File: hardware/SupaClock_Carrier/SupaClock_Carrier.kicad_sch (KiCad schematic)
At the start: 27 parts, among them J11 AD8232_SparkFun, J12_LA1 ECG_LA_pad_M3, J12_RA1 ECG_RA_pad_M3, J12_RL1 ECG_RL_pad_M3, J13 AD8232_Pads_RA_LA_RL, J14 MAX30102_bot, J15 XIAO_BAT_Wires, J3 MAX30102_top, J4 MAX30205_8pad, J5 BMI160_7p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

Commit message: Add DRC JSON files for SupaClock Carrier: drc_post_relax.json and drc_post_thtswap.json
- Created drc_post_relax.json with 509 violations and warnings related to thermal relief, text dimensions, and footprint mismatches.
- Created drc_post_thtswap.json with 653 violations and warnings, including unconnected items, hole size issues, and silkscreen clearance violations.
- Both files include ignored checks and are formatted according to the KiCad DRC schema.
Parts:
- C2: footprint Capacitor_SMD:C_0805_2012Metric_Pad1.18x1.45mm_HandSolder -> Capacitor_THT:CP_Radial_D5.0mm_P2.50mm
- C3, C4, C5, C6: footprint Capacitor_SMD:C_0805_2012Metric_Pad1.18x1.45mm_HandSolder -> Capacitor_THT:C_Disc_D5.0mm_W2.5mm_P5.00mm
- R1, R2, R3, R4, R5: footprint Resistor_SMD:R_0805_2012Metric_Pad1.20x1.40mm_HandSolder -> Resistor_THT:R_Axial_DIN0207_L6.3mm_D2.5mm_P7.62mm_Horizontal
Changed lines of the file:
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@@
 			)
 		)
-		(property "Footprint" "Capacitor_SMD:C_0805_2012Metric_Pad1.18x1.45mm_HandSolder"
+		(property "Footprint" "Capacitor_THT:C_Disc_D5.0mm_W2.5mm_P5.00mm"
 			(at 54.61 43.18 0)
 			(effects
@@
 			)
 		)
-		(property "Footprint" "Resistor_SMD:R_0805_2012Metric_Pad1.20x1.40mm_HandSolder"
+		(property "Footprint" "Resistor_THT:R_Axial_DIN0207_L6.3mm_D2.5mm_P7.62mm_Horizontal"
 			(at 162.56 39.37 0)
 			(effects
@@
 			)
 		)
-		(property "Footprint" "Resistor_SMD:R_0805_2012Metric_Pad1.20x1.40mm_HandSolder"
+		(property "Footprint" "Resistor_THT:R_Axial_DIN0207_L6.3mm_D2.5mm_P7.62mm_Horizontal"
 			(at 72.39 152.4 0)
 			(effects
@@
 			)
 		)
-		(property "Footprint" "Capacitor_SMD:C_0805_2012Metric_Pad1.18x1.45mm_HandSolder"
+		(property "Footprint" "Capacitor_THT:C_Disc_D5.0mm_W2.5mm_P5.00mm"
 			(at 156.21 219.71 0)
 			(effects
@@
 			)
 		)
-		(property "Footprint" "Capacitor_SMD:C_0805_2012Metric_Pad1.18x1.45mm_HandSolder"
+		(property "Footprint" "Capacitor_THT:CP_Radial_D5.0mm_P2.50mm"
 			(at 41.91 43.18 0)
 			(effects
@@
 			)
 		)
-		(property "Footprint" "Capacitor_SMD:C_0805_2012Metric_Pad1.18x1.45mm_HandSolder"
+		(property "Footprint" "Capacitor_THT:C_Disc_D5.0mm_W2.5mm_P5.00mm"
 			(at 171.45 219.71 0)
 			(effects
@@
 			)
 		)
-		(property "Footprint" "Capacitor_SMD:C_0805_2012Metric_Pad1.18x1.45mm_HandSolder"
+		(property "Footprint" "Capacitor_THT:C_Disc_D5.0mm_W2.5mm_P5.00mm"
 			(at 82.55 152.4 0)
 			(effects
@@
 			)
 		)
-		(property "Footprint" "Resistor_SMD:R_0805_2012Metric_Pad1.20x1.40mm_HandSolder"
+		(property "Footprint" "Resistor_THT:R_Axial_DIN0207_L6.3mm_D2.5mm_P7.62mm_Horizontal"
 			(at 130.81 213.36 0)
 			(effects
@@
 			)
 		)
-		(property "Footprint" "Resistor_SMD:R_0805_2012Metric_Pad1.20x1.40mm_HandSolder"
+		(property "Footprint" "Resistor_THT:R_Axial_DIN0207_L6.3mm_D2.5mm_P7.62mm_Horizontal"
 			(at 177.8 39.37 0)
 			(effects
@@
 			)
 		)
-		(property "Footprint" "Resistor_SMD:R_0805_2012Metric_Pad1.20x1.40mm_HandSolder"
+		(property "Footprint" "Resistor_THT:R_Axial_DIN0207_L6.3mm_D2.5mm_P7.62mm_Horizontal"
 			(at 143.51 213.36 0)
 			(effects

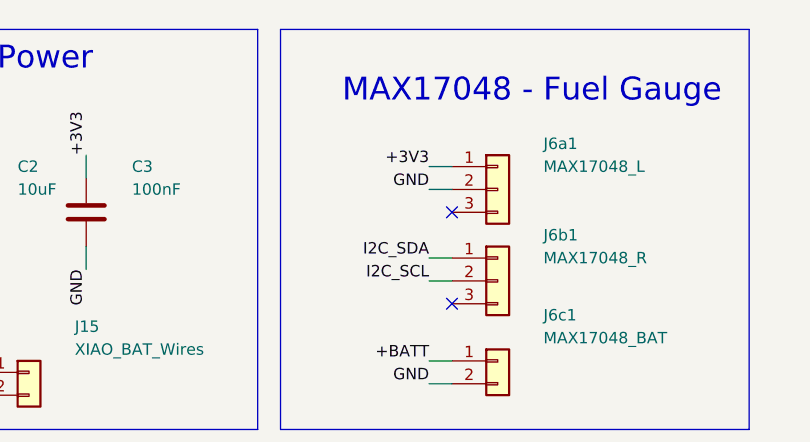
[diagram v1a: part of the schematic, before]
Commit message: Add DRC configuration file for SupaClock Carrier with detailed violation reports
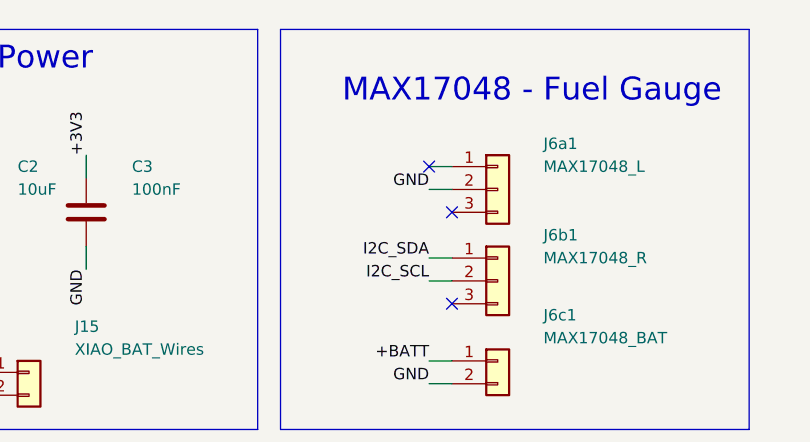
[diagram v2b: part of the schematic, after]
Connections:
- net +3V3: no longer J6a1.1 (Pin_1)
- no-connect marks 10 -> 11

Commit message: nurvos cambios
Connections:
- net +3V3: now also J7.7 (Pin_7); no longer J7.2 (Pin_2)
- net BLK_PWM: now also J7.1 (Pin_1); no longer J7.8 (Pin_8)
- net GND: now also J7.8 (Pin_8); no longer J7.1 (Pin_1)
- net SPI_CS: now also J7.2 (Pin_2); no longer J7.7 (Pin_7)
- net SPI_DC: now also J7.3 (Pin_3); no longer J7.6 (Pin_6)
- net SPI_MOSI: now also J7.5 (Pin_5); no longer J7.4 (Pin_4)
- net SPI_RES: now also J7.4 (Pin_4); no longer J7.5 (Pin_5)
- net SPI_SCK: now also J7.6 (Pin_6); no longer J7.3 (Pin_3)
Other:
- moved on the sheet: J7
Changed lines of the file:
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@@
 	(symbol
 		(lib_id "Connector_Generic:Conn_01x08")
-		(at 59.69 153.67 0)
+		(at 49.53 156.21 180)
 		(unit 1)
 		(body_style 1)
@@
 		(dnp no)
 		(property "Reference" "J7"
-			(at 59.69 139.192 0)
+			(at 49.53 170.688 0)
 			(show_name no)
 			(do_not_autoplace no)
@@
 		)
 		(property "Value" "ST7789_1.69in"
-			(at 51.816 141.478 0)
+			(at 57.404 168.402 0)
 			(show_name no)
 			(do_not_autoplace no)
@@
 		)
 		(property "Footprint" "Connector_PinSocket_2.54mm:PinSocket_1x08_P2.54mm_Vertical"
-			(at 59.69 153.67 0)
+			(at 49.53 156.21 0)
 			(hide yes)
 			(show_name no)
@@
 		)
 		(property "Datasheet" ""
-			(at 59.69 153.67 0)
+			(at 49.53 156.21 0)
 			(hide yes)
 			(show_name no)
@@
 		)
 		(property "Description" ""
-			(at 59.69 153.67 0)
+			(at 49.53 156.21 0)
 			(hide yes)
 			(show_name no)
